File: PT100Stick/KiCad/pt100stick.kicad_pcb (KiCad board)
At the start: 2 copper layers, 15.2 x 20.3 mm, 10 parts, among them U1 MAX31865ATP_

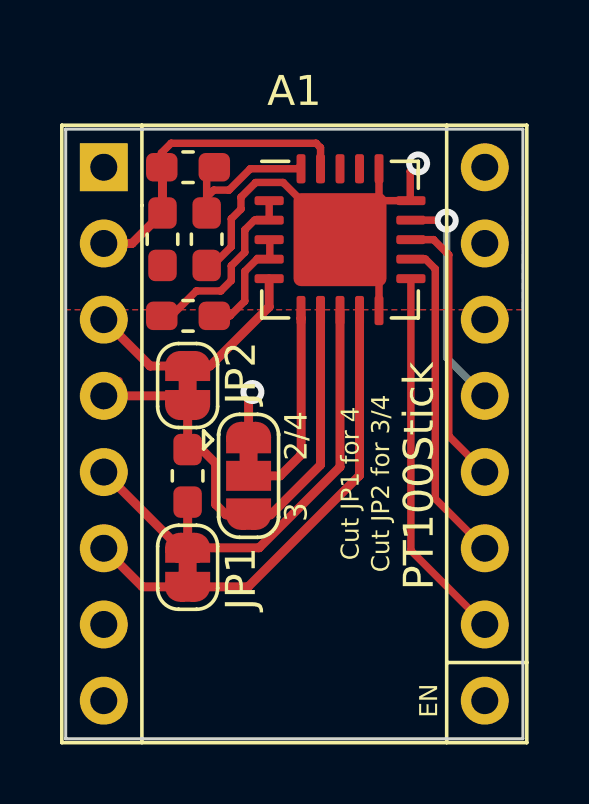
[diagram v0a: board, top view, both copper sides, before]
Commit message: Add 3v3 reg for better board compatibility.
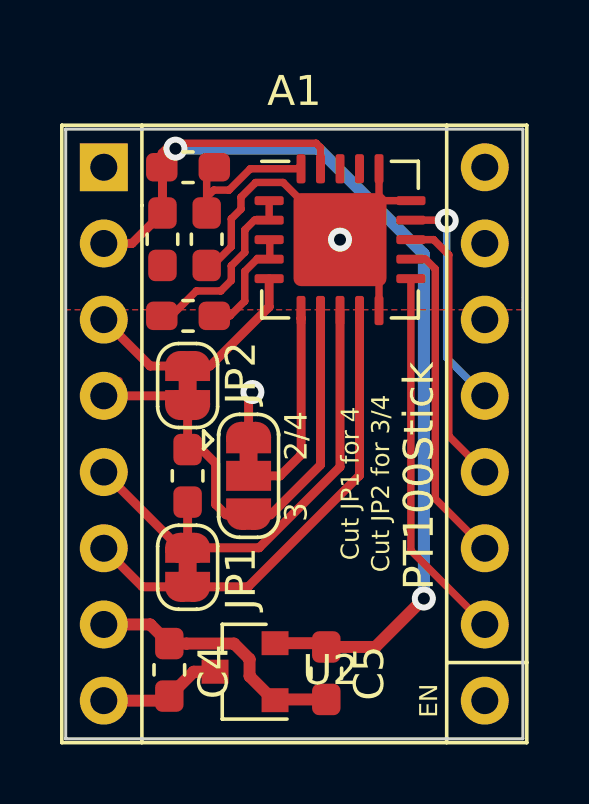
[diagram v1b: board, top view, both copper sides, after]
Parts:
- added C4: 0.1uF, PT100Stick:C_0603_1608Metric_Pad1.05x0.95mm_HandSolder, F.Cu at (144.4, 87.9)
- added C5: 0.1uF, PT100Stick:C_0603_1608Metric_Pad1.05x0.95mm_HandSolder, F.Cu at (149.7, 88.0)
- added U2: MCP1799T-3302H, Package_TO_SOT_SMD:SOT-23, F.Cu at (146.9, 87.9)
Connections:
- A1 pad 2: +3V3 -> Net-(A1-Pad2)
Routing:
- net +3V3: track 10.8 -> 38.4 mm, vias 0 -> 2
- net GND: track 17.1 -> 24.5 mm
- net +24V: track 0.00 -> 4.11 mm

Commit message: Fix 3v3 rail
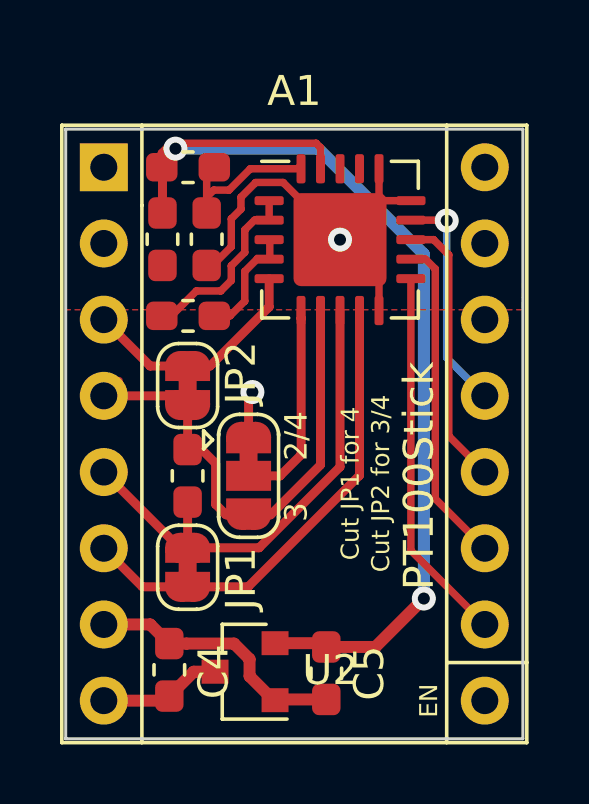
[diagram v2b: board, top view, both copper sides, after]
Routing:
- net +3V3: track 38.4 -> 36.0 mm
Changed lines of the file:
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@@
-(kicad_pcb (version 20171130) (host pcbnew "(5.1.4)-1")
+(kicad_pcb (version 20171130) (host pcbnew "(5.1.5)-3")
   (general
     (thickness 1.6)
     (drawings 33)
-    (tracks 132)
+    (tracks 130)
     (zones 0)
     (modules 13)
@@
   )
   (setup
-    (last_trace_width 0.4)
+    (last_trace_width 0.25)
     (user_trace_width 0.3)
     (user_trace_width 0.4)
@@
   (segment (start 144.159 71.12) (end 144.159 70.645) (width 0.25) (layer F.Cu) (net 6) (status 30))
   (segment (start 144.173 71.32349) (end 144.173 71.12) (width 0.25) (layer F.Cu) (net 6) (status 30))
-  (segment (start 143.1798 73.66) (end 144.1958 72.644) (width 0.3) (layer F.Cu) (net 6) (status 20))
-  (segment (start 142.24 73.66) (end 143.1798 73.66) (width 0.3) (layer F.Cu) (net 6) (status 10))
   (segment (start 144.1958 71.1428) (end 144.173 71.12) (width 0.3) (layer F.Cu) (net 6) (status 30))
   (segment (start 144.1958 72.644) (end 144.1958 71.1428) (width 0.3) (layer F.Cu) (net 6) (status 30))
